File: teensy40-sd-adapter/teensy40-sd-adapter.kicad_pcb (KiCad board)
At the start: 2 copper layers, 11.4 x 12.2 mm, 3 parts, among them J1 Micro_SD_Card_Det_Single, J2 Conn_01x08

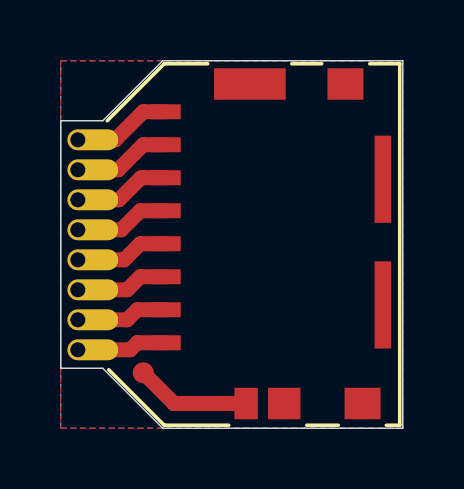
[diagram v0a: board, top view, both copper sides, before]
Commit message: Move files and redesign for fab with castellated holes
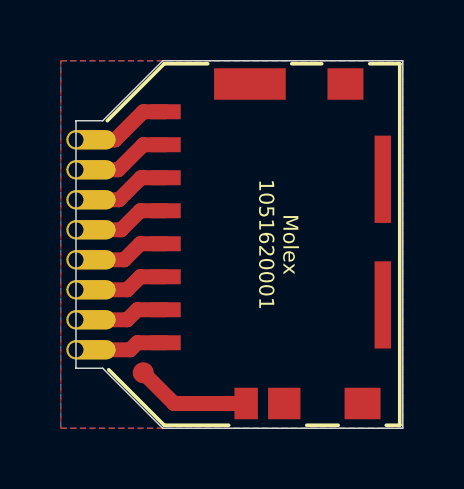
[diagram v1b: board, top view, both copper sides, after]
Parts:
- moved J2 0.06 mm to (125.3, 91.7)
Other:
- board size 11.4 x 12.2 mm -> 10.9 x 12.2 mm
- net class Default: clearance 0.2 -> 0.05
- rule pad_to_mask_clearance: 0.051 -> 0.0508
- rule solder_mask_min_width: 0.25 -> 0.1016
- rule trace_clearance: 0.2 -> 0.05
- board text added: "Molex 1051620001"
- board text removed: "FILE AWAY EDGE TO MAKE CASTELLATIONS"
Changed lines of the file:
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@@
   (general
     (thickness 1.6)
-    (drawings 37)
+    (drawings 42)
     (tracks 28)
     (zones 0)
@@
   (setup
     (last_trace_width 0.5)
-    (trace_clearance 0.2)
+    (trace_clearance 0.05)
     (zone_clearance 0.508)
     (zone_45_only no)
@@
     (pad_size 0.75 0.75)
     (pad_drill 0)
-    (pad_to_mask_clearance 0.051)
-    (solder_mask_min_width 0.25)
+    (pad_to_mask_clearance 0.0508)
+    (solder_mask_min_width 0.1016)
     (aux_axis_origin 0 0)
+    (grid_origin 124.75 101.35)
     (visible_elements 7FFFFFFF)
     (pcbplotparams
-      (layerselection 0x010fc_ffffffff)
-      (usegerberextensions false)
+      (layerselection 0x010f0_ffffffff)
+      (usegerberextensions true)
       (usegerberattributes false)
       (usegerberadvancedattributes false)
@@
       (viasonmask false)
       (mode 1)
-      (useauxorigin false)
+      (useauxorigin true)
       (hpglpennumber 1)
       (hpglpenspeed 20)
@@
       (outputformat 1)
       (mirror false)
-      (drillshape 1)
+      (drillshape 0)
       (scaleselection 1)
-      (outputdirectory ""))
+      (outputdirectory "gerber/"))
   )
   (net 0 "")
@@
   (net 9 /CLK)
   (net_class Default "This is the default net class."
-    (clearance 0.2)
+    (clearance 0.05)
     (trace_width 0.5)
     (via_dia 0.8)
@@
     (add_net "Net-(J1-Pad9)")
   )
+  (module nibelung:Teensy40_SD_Castellated (layer F.Cu)
+    (at 125.258 91.735001)
+    (descr "Castellated holes for SD card adapter for pads on Teensy 4.0 bottom")
+    (fp_text reference J2 (at 0 9) (layer F.SilkS) hide
+      (effects (font (size 1 1) (thickness 0.15)))
+    )
+    (fp_text value Conn_01x08 (at 0 -1.5) (layer F.Fab) hide
+      (effects (font (size 1 1) (thickness 0.15)))
+    )
+    (fp_line (start 1.5 8) (end -0.5 8) (layer F.CrtYd) (width 0.05))
+    (fp_line (start 1.5 -1) (end 1.5 8) (layer F.CrtYd) (width 0.05))
+    (fp_line (start -0.5 -1) (end 1.5 -1) (layer F.CrtYd) (width 0.05))
+    (fp_line (start -0.5 8) (end -0.5 -1) (layer F.CrtYd) (width 0.05))
+    (fp_line (start 0 -0.5) (end 0 7.5) (layer F.CrtYd) (width 0.12))
+    (pad 8 thru_hole roundrect (at 0 7) (size 1.65 0.65) (drill 0.5 (offset 0.5 0)) (layers *.Cu *.Mask) (roundrect_rratio 0.5)
+      (net 8 /DAT2))
+    (pad 7 thru_hole roundrect (at 0 6) (size 1.65 0.65) (drill 0.5 (offset 0.5 0)) (layers *.Cu *.Mask) (roundrect_rratio 0.5)
+      (net 7 /DAT3))
+    (pad 6 thru_hole roundrect (at 0 5) (size 1.65 0.65) (drill 0.5 (offset 0.5 0)) (layers *.Cu *.Mask) (roundrect_rratio 0.5)
+      (net 6 /CMD))
+    (pad 5 thru_hole roundrect (at 0 4) (size 1.65 0.65) (drill 0.5 (offset 0.5 0)) (layers *.Cu *.Mask) (roundrect_rratio 0.5)
+      (net 5 /VDD))
+    (pad 4 thru_hole roundrect (at 0 3) (size 1.65 0.65) (drill 0.5 (offset 0.5 0)) (layers *.Cu *.Mask) (roundrect_rratio 0.5)
+      (net 9 /CLK))
+    (pad 3 thru_hole roundrect (at 0 2) (size 1.65 0.65) (drill 0.5 (offset 0.5 0)) (layers *.Cu *.Mask) (roundrect_rratio 0.5)
+      (net 4 /VSS))
+    (pad 2 thru_hole roundrect (at 0 1) (size 1.65 0.65) (drill 0.5 (offset 0.5 0)) (layers *.Cu *.Mask) (roundrect_rratio 0.5)
+      (net 3 /DAT0))
+    (pad 1 thru_hole roundrect (at 0 0) (size 1.65 0.65) (drill 0.5 (offset 0.5 0)) (layers *.Cu *.Mask) (roundrect_rratio 0.5)
+      (net 2 /DAT1))
+  )
   (module nibelung:Pad_0.7mm (layer F.Cu)
     (at 127.5 99.5)
@@
     (pad 1 smd circle (at 0 0) (size 0.7 0.7) (layers F.Cu F.Paste F.Mask)
       (net 1 "Net-(J1-Pad9)") (solder_mask_margin 0.03))
-  )
-  (module nibelung:Teensy40_SD_Castellated (layer F.Cu)
-    (at 125.32 91.735001)
-    (descr "Castellated holes for SD card adapter for pads on Teensy 4.0 bottom")
-    (fp_text reference J2 (at 0 9) (layer F.SilkS) hide
-      (effects (font (size 1 1) (thickness 0.15)))
-    )
-    (fp_text value Conn_01x08 (at 0 -1.5) (layer F.Fab) hide
-      (effects (font (size 1 1) (thickness 0.15)))
-    )
-    (fp_line (start 0 -0.5) (end 0 7.5) (layer F.CrtYd) (width 0.12))
-    (pad 8 thru_hole roundrect (at 0 7) (size 1.7 0.7) (drill 0.5 (offset 0.5 0)) (layers *.Cu *.Mask) (roundrect_rratio 0.5)
-      (net 8 /DAT2) (solder_mask_margin 0.03))
-    (pad 7 thru_hole roundrect (at 0 6) (size 1.7 0.7) (drill 0.5 (offset 0.5 0)) (layers *.Cu *.Mask) (roundrect_rratio 0.5)
-      (net 7 /DAT3) (solder_mask_margin 0.03))
-    (pad 6 thru_hole roundrect (at 0 5) (size 1.7 0.7) (drill 0.5 (offset 0.5 0)) (layers *.Cu *.Mask) (roundrect_rratio 0.5)
-      (net 6 /CMD) (solder_mask_margin 0.03))
-    (pad 5 thru_hole roundrect (at 0 4) (size 1.7 0.7) (drill 0.5 (offset 0.5 0)) (layers *.Cu *.Mask) (roundrect_rratio 0.5)
-      (net 5 /VDD) (solder_mask_margin 0.03))
-    (pad 4 thru_hole roundrect (at 0 3) (size 1.7 0.7) (drill 0.5 (offset 0.5 0)) (layers *.Cu *.Mask) (roundrect_rratio 0.5)
-      (net 9 /CLK) (solder_mask_margin 0.03))
-    (pad 3 thru_hole roundrect (at 0 2) (size 1.7 0.7) (drill 0.5 (offset 0.5 0)) (layers *.Cu *.Mask) (roundrect_rratio 0.5)
-      (net 4 /VSS) (solder_mask_margin 0.03))
-    (pad 2 thru_hole roundrect (at 0 1) (size 1.7 0.7) (drill 0.5 (offset 0.5 0)) (layers *.Cu *.Mask) (roundrect_rratio 0.5)
-      (net 3 /DAT0) (solder_mask_margin 0.03))
-    (pad 1 thru_hole roundrect (at 0 0) (size 1.7 0.7) (drill 0.5 (offset 0.5 0)) (layers *.Cu *.Mask) (roundrect_rratio 0.5)
-      (net 2 /DAT1) (solder_mask_margin 0.03))
   )
   (module nibelung:microSD_Molex_1051620001 (layer F.Cu)
@@
       (net 8 /DAT2))
   )
+  (gr_text "Molex\n1051620001" (at 132 95.225 270) (layer F.SilkS)
+    (effects (font (size 0.5 0.5) (thickness 0.1)))
+  )
+  (gr_line (start 126.3 91.1) (end 128.2 89.2) (layer B.SilkS) (width 0.12))
+  (gr_line (start 128.2 89.2) (end 136.05 89.2) (layer B.SilkS) (width 0.12))
+  (gr_line (start 136.05 89.2) (end 136.05 101.25) (layer B.SilkS) (width 0.12))
+  (gr_line (start 136.05 101.25) (end 128.2 101.25) (layer B.SilkS) (width 0.12))
+  (gr_line (start 128.2 101.25) (end 126.35 99.4) (layer B.SilkS) (width 0.12))
   (gr_line (start 151.75 95.75) (end 152.5 95) (layer Cmts.User) (width 0.15))
   (gr_line (start 152.5 95) (end 151.75 94.25) (layer Cmts.User) (width 0.15))
@@
   (gr_line (start 128.2 89.2) (end 129.65 89.2) (layer F.SilkS) (width 0.12))
   (gr_line (start 126.3 91.1) (end 128.2 89.2) (layer F.SilkS) (width 0.12))
-  (gr_text "Teensy 4.0\nmicroSD\nAdapter" (at 131 95 270) (layer B.SilkS)
+  (gr_text "Teensy 4.0\nmicroSD\nAdapter" (at 131.25 95.225 270) (layer B.SilkS)
     (effects (font (size 1 1) (thickness 0.15)) (justify mirror))
   )
-  (gr_line (start 124.75 99.35) (end 124.75 91.1) (layer Edge.Cuts) (width 0.05))
-  (gr_line (start 126.15 99.35) (end 124.75 99.35) (layer Edge.Cuts) (width 0.05))
+  (gr_line (start 125.258 99.35) (end 125.258 91.1) (layer Edge.Cuts) (width 0.05))
+  (gr_line (start 126.15 99.35) (end 125.258 99.35) (layer Edge.Cuts) (width 0.05))
   (gr_line (start 128.15 101.35) (end 126.15 99.35) (layer Edge.Cuts) (width 0.05))
   (gr_line (start 136.15 101.35) (end 128.15 101.35) (layer Edge.Cuts) (width 0.05))
@@
   (gr_line (start 128.15 89.1) (end 136.15 89.1) (layer Edge.Cuts) (width 0.05))
   (gr_line (start 126.15 91.1) (end 128.15 89.1) (layer Edge.Cuts) (width 0.05))
-  (gr_line (start 124.75 91.1) (end 126.15 91.1) (layer Edge.Cuts) (width 0.05))
-  (gr_text "FILE AWAY EDGE\nTO MAKE \nCASTELLATIONS" (at 115.75 95.25) (layer Cmts.User)
-    (effects (font (size 1 1) (thickness 0.15)))
-  )
+  (gr_line (start 125.258 91.1) (end 126.15 91.1) (layer Edge.Cuts) (width 0.05))
   (dimension 12.25 (width 0.15) (layer Dwgs.User)
     (gr_text "12.250 mm" (at 139.45 95.225 270) (layer Dwgs.User)
@@
     (arrow2b (pts (xy 138.15 89.1) (xy 138.736421 90.226504)))
   )
-  (dimension 11.5 (width 0.15) (layer Dwgs.User)
-    (gr_text "11.500 mm" (at 130.4 85.8) (layer Dwgs.User)
+  (dimension 10.9 (width 0.15) (layer Dwgs.User)
+    (gr_text "10.900 mm" (at 130.7 85.8) (layer Dwgs.User)
       (effects (font (size 1 1) (thickness 0.15)))
     )
     (feature1 (pts (xy 136.15 88.1) (xy 136.15 86.513579)))
-    (feature2 (pts (xy 124.65 88.1) (xy 124.65 86.513579)))
-    (crossbar (pts (xy 124.65 87.1) (xy 136.15 87.1)))
+    (feature2 (pts (xy 125.25 88.1) (xy 125.25 86.513579)))
+    (crossbar (pts (xy 125.25 87.1) (xy 136.15 87.1)))
     (arrow1a (pts (xy 136.15 87.1) (xy 135.023496 87.686421)))
     (arrow1b (pts (xy 136.15 87.1) (xy 135.023496 86.513579)))
-    (arrow2a (pts (xy 124.65 87.1) (xy 125.776504 87.686421)))
-    (arrow2b (pts (xy 124.65 87.1) (xy 125.776504 86.513579)))
+    (arrow2a (pts (xy 125.25 87.1) (xy 126.376504 87.686421)))
+    (arrow2b (pts (xy 125.25 87.1) (xy 126.376504 86.513579)))
   )
   (gr_line (start 136.15 89.1) (end 124.75 89.1) (layer Dwgs.User) (width 0.05))
@@
   (segment (start 127.424975 93) (end 127.5 93) (width 0.5) (layer F.Cu) (net 4))
   (segment (start 126.689974 93.735001) (end 127.424975 93) (width 0.5) (layer F.Cu) (net 4))
-  (segment (start 125.32 94.735001) (end 126.764999 94.735001) (width 0.5) (layer F.Cu) (net 9))
-  (segment (start 127.4 94.1) (end 128.25 94.1) (width 0.5) (layer F.Cu) (net 9))
-  (segment (start 126.764999 94.735001) (end 127.4 94.1) (width 0.5) (layer F.Cu) (net 9))
   (segment (start 127.4 95.2) (end 128.25 95.2) (width 0.5) (layer F.Cu) (net 5))
   (segment (start 125.32 95.735001) (end 126.864999 95.735001) (width 0.5) (layer F.Cu) (net 5))
@@
   (segment (start 127.3 98.5) (end 128.25 98.5) (width 0.5) (layer F.Cu) (net 8))
   (segment (start 127.064999 98.735001) (end 127.3 98.5) (width 0.5) (layer F.Cu) (net 8))
+  (segment (start 125.32 94.735001) (end 126.764999 94.735001) (width 0.5) (layer F.Cu) (net 9))
+  (segment (start 127.4 94.1) (end 128.25 94.1) (width 0.5) (layer F.Cu) (net 9))
+  (segment (start 126.764999 94.735001) (end 127.4 94.1) (width 0.5) (layer F.Cu) (net 9))
   (zone (net 0) (net_name "") (layer B.Cu) (hatch edge 0.508)
     (connect_pads (clearance 0.508))
